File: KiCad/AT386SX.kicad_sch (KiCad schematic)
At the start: 31 parts, among them J10 OSC_PIN1, J11 OSC_PIN8, Q3 2N3904, U2 74HC05, U6 ICW42C07, U7 Cx486SLC, U8 80387SX, U9 RC2016A5, X2 14.31818MHz

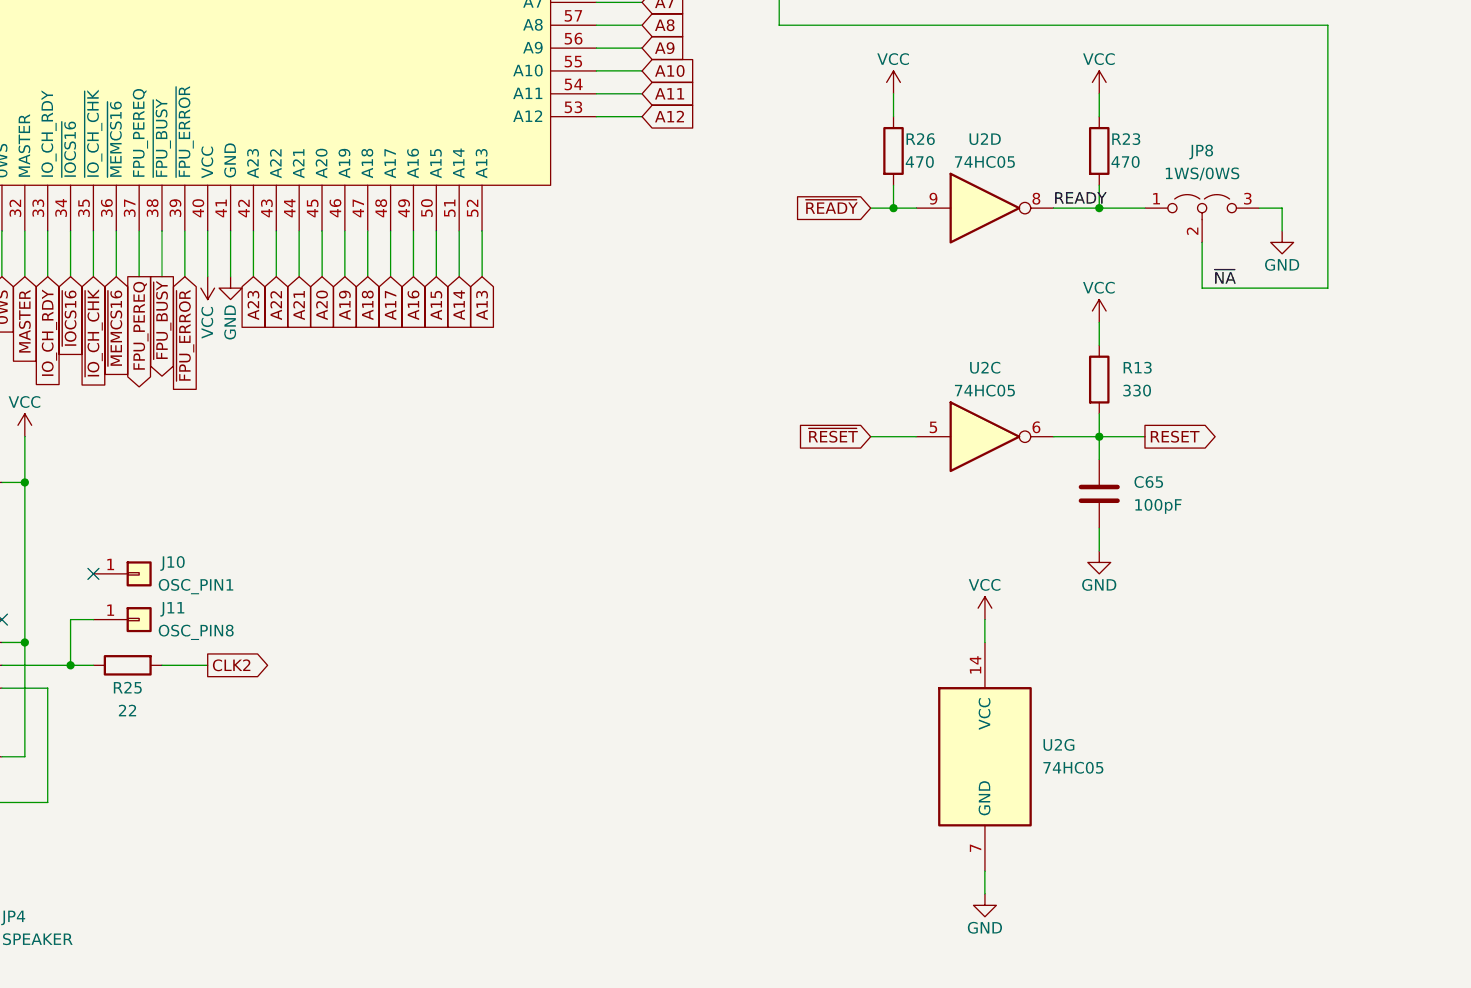
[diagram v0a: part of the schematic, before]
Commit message: Add R32, update footprints
Signed-off-by: Sergey Kiselev <skiselev@gmail.com>
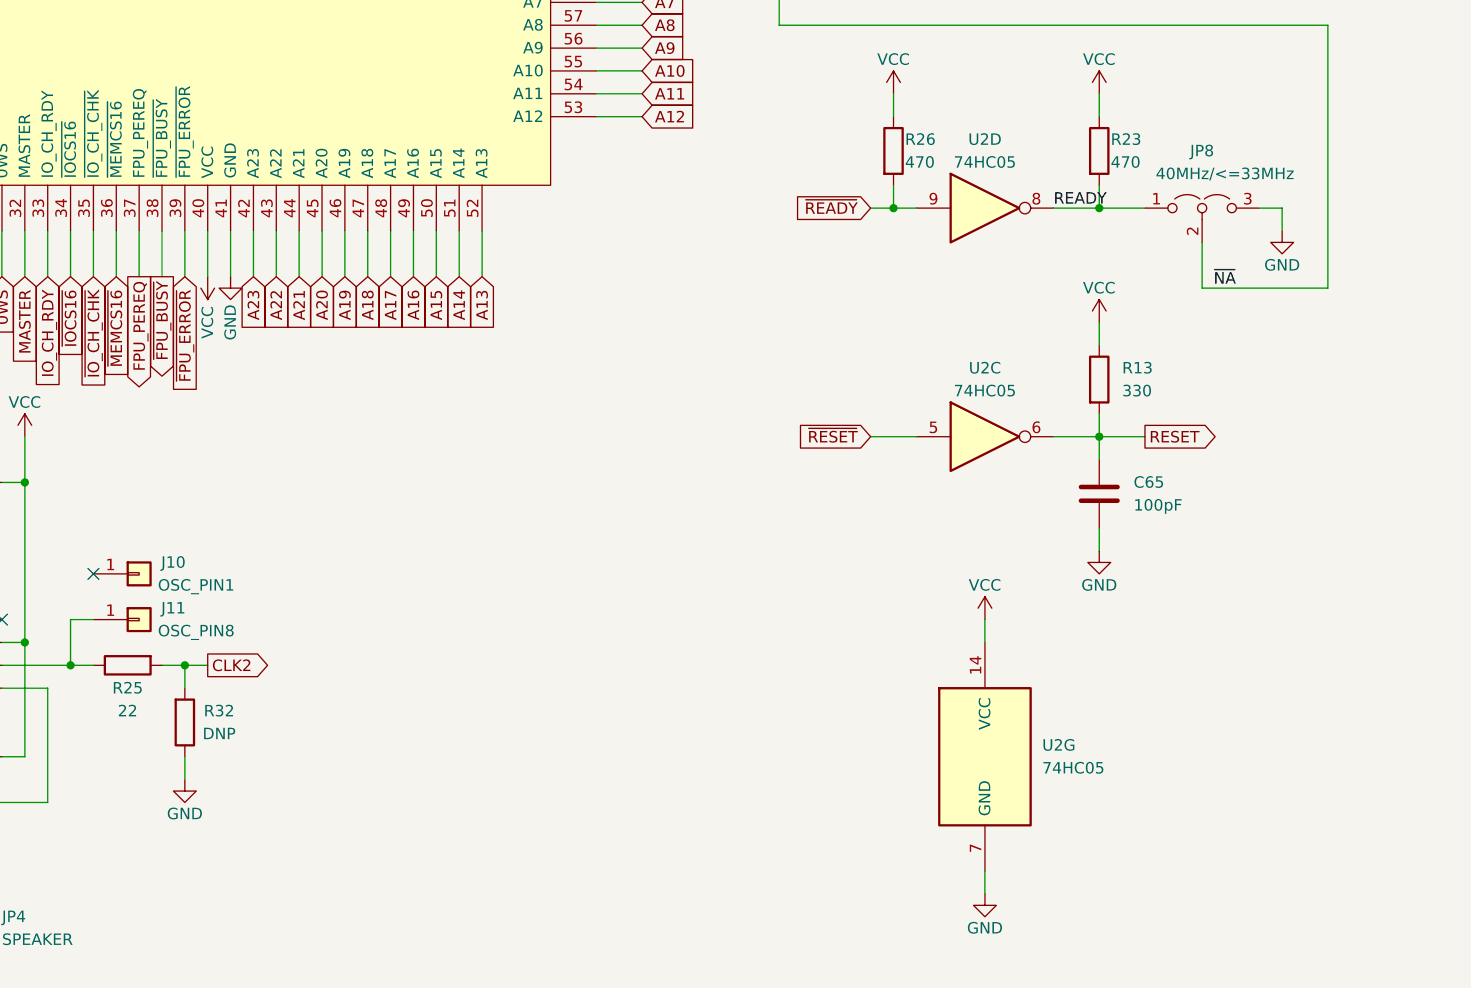
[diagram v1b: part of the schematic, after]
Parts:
- added R32: DNP, My_Components:Res_Axial_L6.3mm_D2.5mm_P10.16mm_Horizontal, symbol Device:R
- JP8: value 1WS/0WS -> 40MHz/<=33MHz
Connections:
- net CLK2: now also R32.2
- net GND: now also R32.1
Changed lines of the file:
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@@
   (junction (at 76.2 233.68) (diameter 0) (color 0 0 0 0)
   )
+  (junction (at 139.7 238.76) (diameter 0) (color 0 0 0 0)
+  )
   (junction (at 351.79 40.64) (diameter 0) (color 0 0 0 0)
   )
@@
     (stroke (width 0) (type default) (color 0 0 0 0))
   )
-  (wire (pts (xy 142.24 238.76) (xy 137.16 238.76))
+  (wire (pts (xy 142.24 238.76) (xy 139.7 238.76))
     (stroke (width 0) (type default) (color 0 0 0 0))
   )
@@
     (stroke (width 0) (type default) (color 0 0 0 0))
   )
+  (wire (pts (xy 139.7 238.76) (xy 137.16 238.76))
+    (stroke (width 0) (type default) (color 0 0 0 0))
+  )
   (wire (pts (xy 247.65 43.18) (xy 247.65 40.64))
     (stroke (width 0) (type default) (color 0 0 0 0))
@@
     (stroke (width 0) (type default) (color 0 0 0 0))
   )
+  (wire (pts (xy 139.7 248.92) (xy 139.7 251.46))
+    (stroke (width 0) (type default) (color 0 0 0 0))
+  )
   (wire (pts (xy 81.28 35.56) (xy 81.28 30.48))
     (stroke (width 0) (type default) (color 0 0 0 0))
@@
     (stroke (width 0) (type default) (color 0 0 0 0))
   )
+  (wire (pts (xy 139.7 238.76) (xy 139.7 241.3))
+    (stroke (width 0) (type default) (color 0 0 0 0))
+  )
   (wire (pts (xy 292.1 93.98) (xy 297.18 93.98))
     (stroke (width 0) (type default) (color 0 0 0 0))
@@
     (pin "1")
   )
+  (symbol (lib_id "power:GND") (at 139.7 251.46 0) (unit 1)
+    (in_bom yes) (on_board yes)
+    (property "Reference" "#PWR0223" (id 0) (at 139.7 257.81 0)
+      (effects (font (size 1.27 1.27)) hide)
+    )
+    (property "Value" "GND" (id 1) (at 139.7 255.27 0))
+    (property "Footprint" "" (id 2) (at 139.7 251.46 0)
+      (effects (font (size 1.27 1.27)) hide)
+    )
+    (property "Datasheet" "" (id 3) (at 139.7 251.46 0)
+      (effects (font (size 1.27 1.27)) hide)
+    )
+    (pin "1")
+  )
+  (symbol (lib_id "Device:R") (at 139.7 245.11 0) (mirror x) (unit 1)
+    (in_bom yes) (on_board yes)
+    (property "Reference" "R32" (id 0) (at 143.51 243.84 0))
+    (property "Value" "DNP" (id 1) (at 143.51 246.38 0))
+    (property "Footprint" "My_Components:Res_Axial_L6.3mm_D2.5mm_P10.16mm_Horizontal" (id 2) (at 137.922 245.11 90)
+      (effects (font (size 1.27 1.27)) hide)
+    )
+    (property "Datasheet" "~" (id 3) (at 139.7 245.11 0)
+      (effects (font (size 1.27 1.27)) hide)
+    )
+    (pin "1")
+    (pin "2")
+  )
   (symbol (lib_id "Device:C") (at 292.1 177.8 0) (unit 1)
     (in_bom yes) (on_board yes)
@@
   )
   (symbol (lib_id "Jumper:Jumper_3_Open") (at 252.73 187.96 0) (unit 1)
-    (in_bom yes) (on_board yes) (fields_autoplaced)
+    (in_bom yes) (on_board yes)
     (property "Reference" "JP8" (id 0) (at 252.73 181.61 0))
-    (property "Value" "1WS/0WS" (id 1) (at 252.73 184.15 0))
+    (property "Value" "40MHz/<=33MHz" (id 1) (at 255.27 184.15 0))
     (property "Footprint" "My_Components:Conn_Pin_Header_3x1_2.54mm" (id 2) (at 252.73 187.96 0)
       (effects (font (size 1.27 1.27)) hide)
@@
       (reference "#PWR0222") (unit 1) (value "VCC") (footprint "")
     )
+    (path "/55ed73a7-51dc-499f-b11a-5ec63d0d43a0"
+      (reference "#PWR0223") (unit 1) (value "GND") (footprint "")
+    )
     (path "/1c0f074e-275c-4c09-93e3-0959df27fb02/86b1cd36-634b-40d3-be88-938fc26678f7"
-      (reference "BT1") (unit 1) (value "Battery") (footprint "My_Components:Battery_Varta_3V80H")
+      (reference "BT1") (unit 1) (value "Varta 3/V80H") (footprint "My_Components:Battery_Varta_3V80H")
     )
     (path "/b540f997-cabb-4061-85a0-370b4e9dd03a/00000000-0000-0000-0000-000063401a80"
@@
     )
     (path "/779afa25-ee57-4270-917a-2000de0bd30f"
-      (reference "JP8") (unit 1) (value "1WS/0WS") (footprint "My_Components:Conn_Pin_Header_3x1_2.54mm")
+      (reference "JP8") (unit 1) (value "40MHz/<=33MHz") (footprint "My_Components:Conn_Pin_Header_3x1_2.54mm")
     )
     (path "/b0ba3ef2-6446-43a3-bd27-b206e256e775"
@@
       (reference "R31") (unit 1) (value "1k") (footprint "My_Components:Res_Axial_L6.3mm_D2.5mm_P10.16mm_Horizontal")
     )
+    (path "/56ab2f9d-f360-4763-a520-1236cf082aa2"
+      (reference "R32") (unit 1) (value "DNP") (footprint "My_Components:Res_Axial_L6.3mm_D2.5mm_P10.16mm_Horizontal")
+    )
     (path "/b540f997-cabb-4061-85a0-370b4e9dd03a/15c5cb70-9076-4d0d-8d62-4d5b5f0b4f83"
       (reference "RP1") (unit 1) (value "4.7k") (footprint "My_Components:Conn_SIL9")
@@
     )
     (path "/1c0f074e-275c-4c09-93e3-0959df27fb02/937700a1-26dd-490c-ae66-0b7e3939b8e2"
-      (reference "U10") (unit 1) (value "SIMM0") (footprint "My_Components:Conn_SIMM30")
+      (reference "U10") (unit 1) (value "BANK0") (footprint "My_Components:Conn_SIMM30")
     )
     (path "/1c0f074e-275c-4c09-93e3-0959df27fb02/a2af9dba-42df-4812-8663-360a4f93771d"
-      (reference "U11") (unit 1) (value "SIMM1") (footprint "My_Components:Conn_SIMM30")
+      (reference "U11") (unit 1) (value "BANK0") (footprint "My_Components:Conn_SIMM30")
     )
     (path "/1c0f074e-275c-4c09-93e3-0959df27fb02/0bfae472-811c-4887-9df9-78a9ee9a7876"
-      (reference "U12") (unit 1) (value "SIMM2") (footprint "My_Components:Conn_SIMM30")
+      (reference "U12") (unit 1) (value "BANK1") (footprint "My_Components:Conn_SIMM30")
     )
     (path "/1c0f074e-275c-4c09-93e3-0959df27fb02/069056e6-b6c0-4250-b4d3-e0552f9a5620"
-      (reference "U13") (unit 1) (value "SIMM3") (footprint "My_Components:Conn_SIMM30")
+      (reference "U13") (unit 1) (value "BANK1") (footprint "My_Components:Conn_SIMM30")
     )
     (path "/1c0f074e-275c-4c09-93e3-0959df27fb02/19834531-ffc0-44fe-9d79-92a55a925e18"

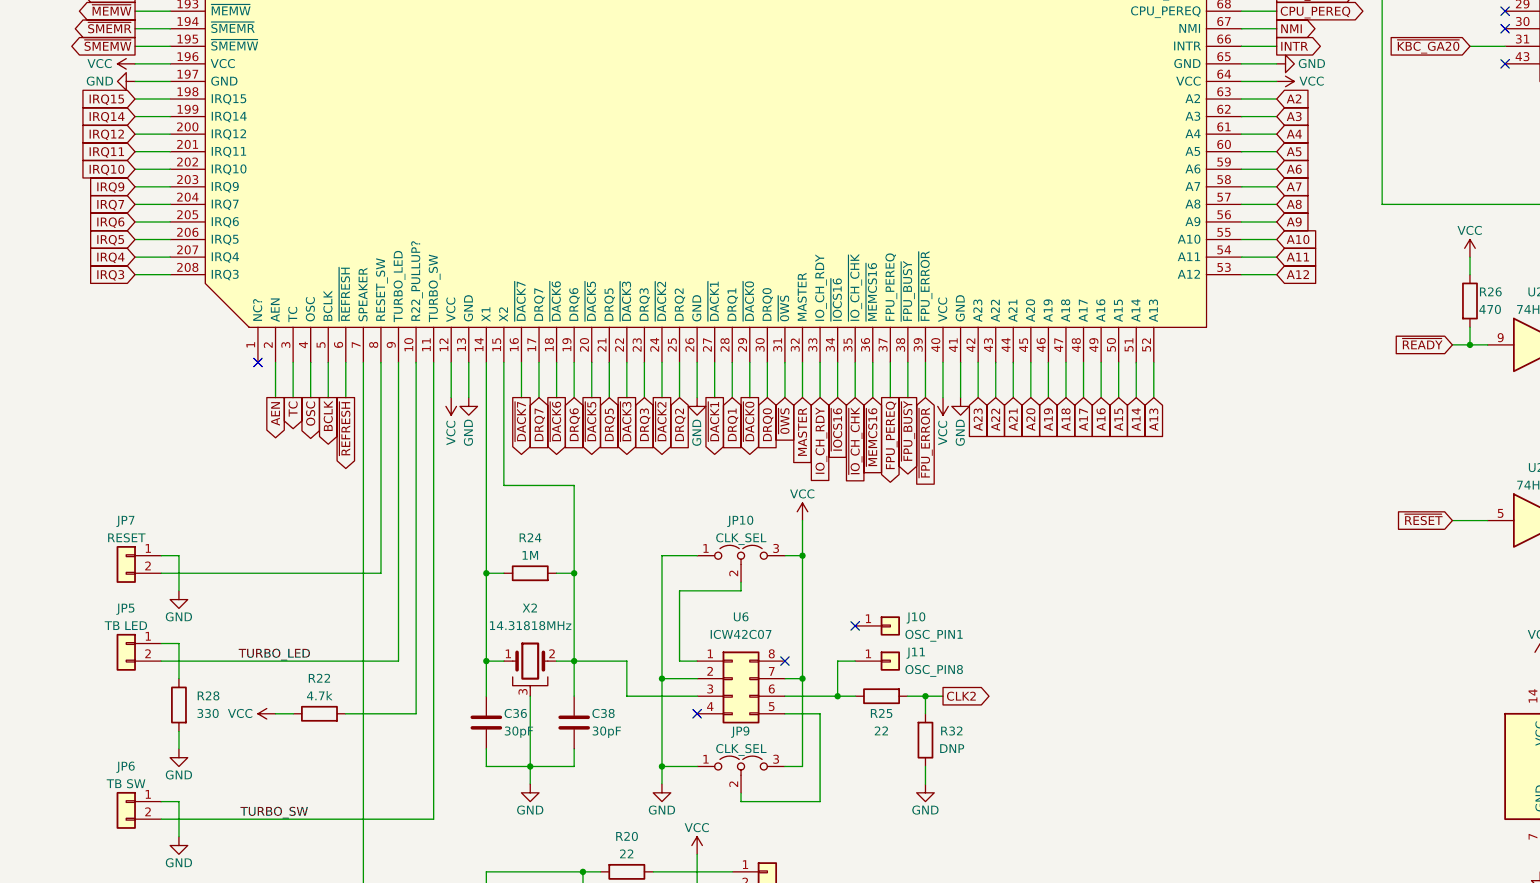
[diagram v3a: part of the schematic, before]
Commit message: Version 1.3: Implement PS/2 mouse. Use PS/2 dualport pinout for the keyboard/mouse connector
Signed-off-by: Sergey Kiselev <skiselev@gmail.com>
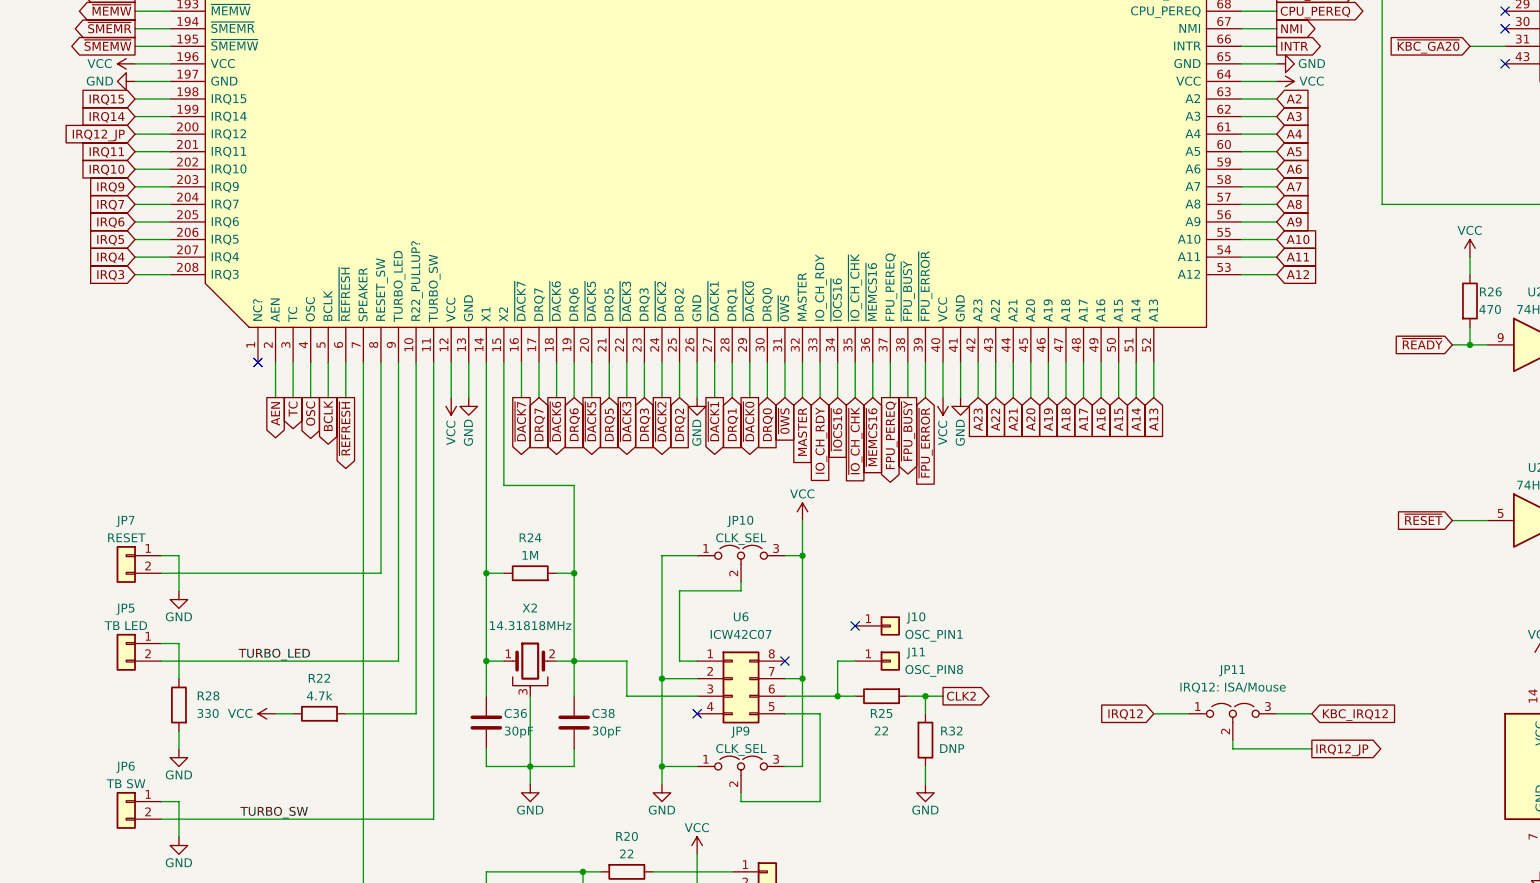
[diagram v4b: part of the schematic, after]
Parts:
- added JP11: IRQ12: ISA/Mouse, My_Components:Conn_Pin_Header_3x1_2.54mm, symbol Jumper:Jumper_3_Open
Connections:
- net IRQ12: now also JP11.1 (A); no longer U9.200 (IRQ12)
- new net IRQ12_JP: JP11.2 (C), U9.200 (IRQ12)
- new net KBC_IRQ12: JP11.3 (B)
